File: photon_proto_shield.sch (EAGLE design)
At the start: 15 parts

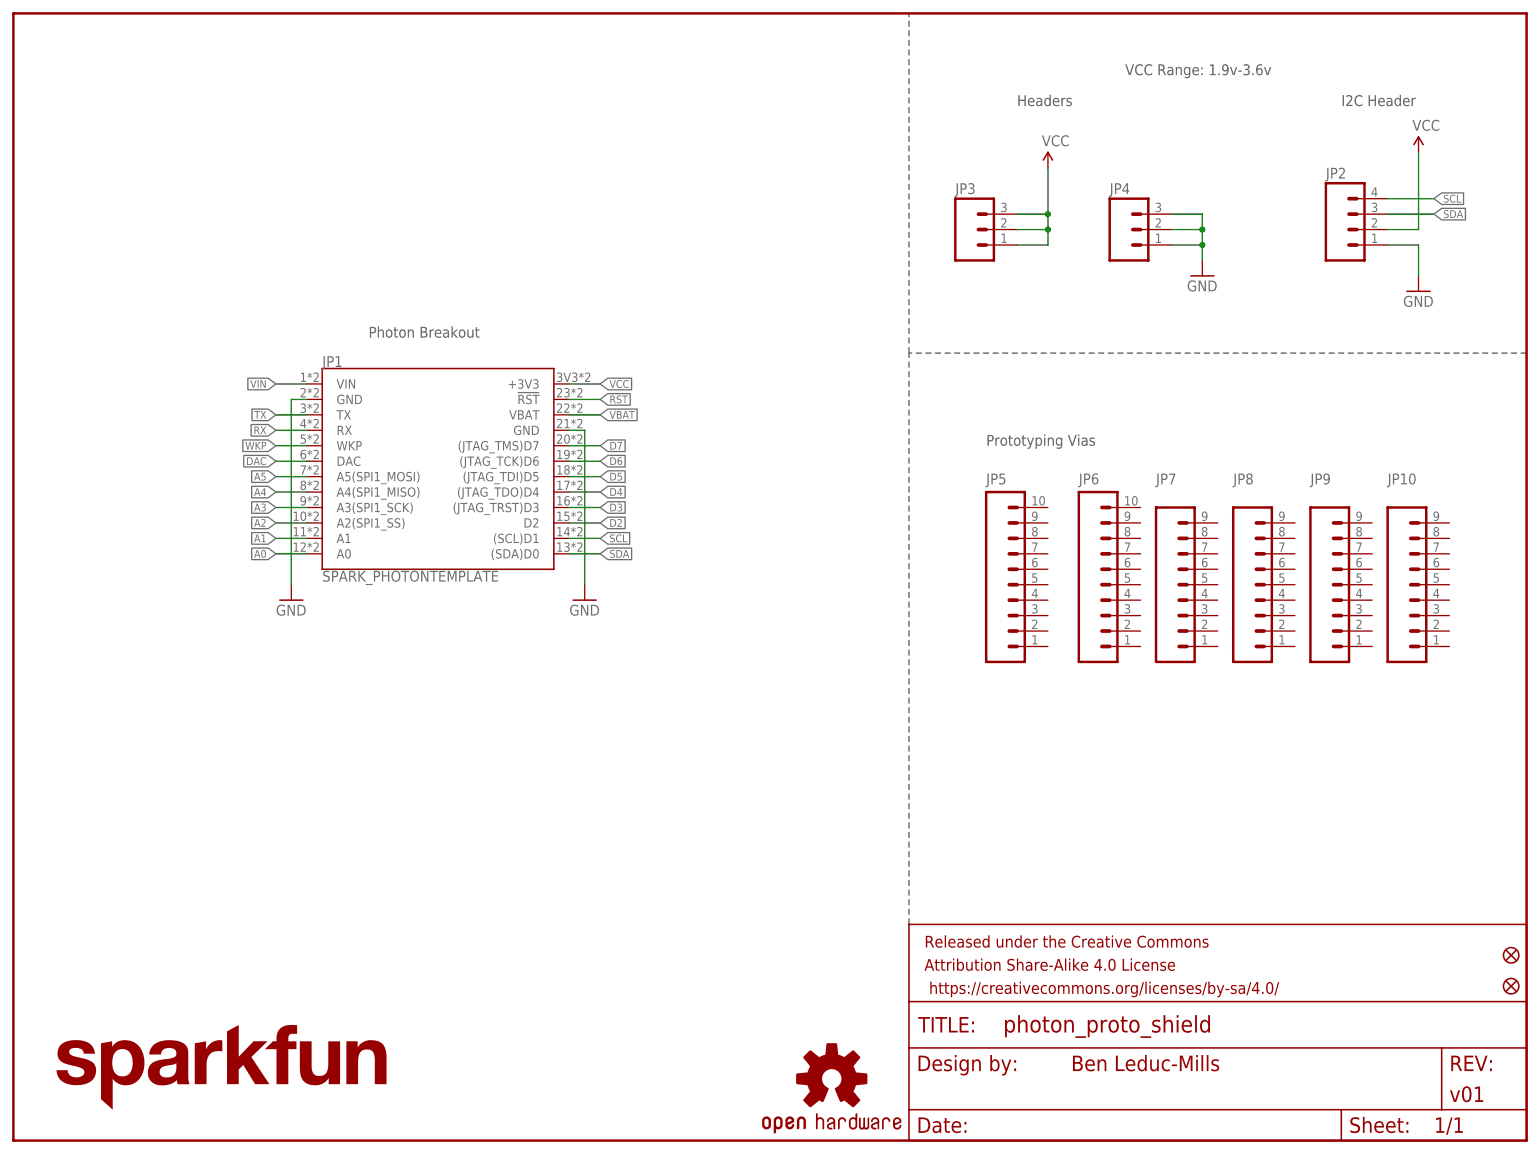
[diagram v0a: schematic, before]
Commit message: Adding gap between Photon and pin breakouts.
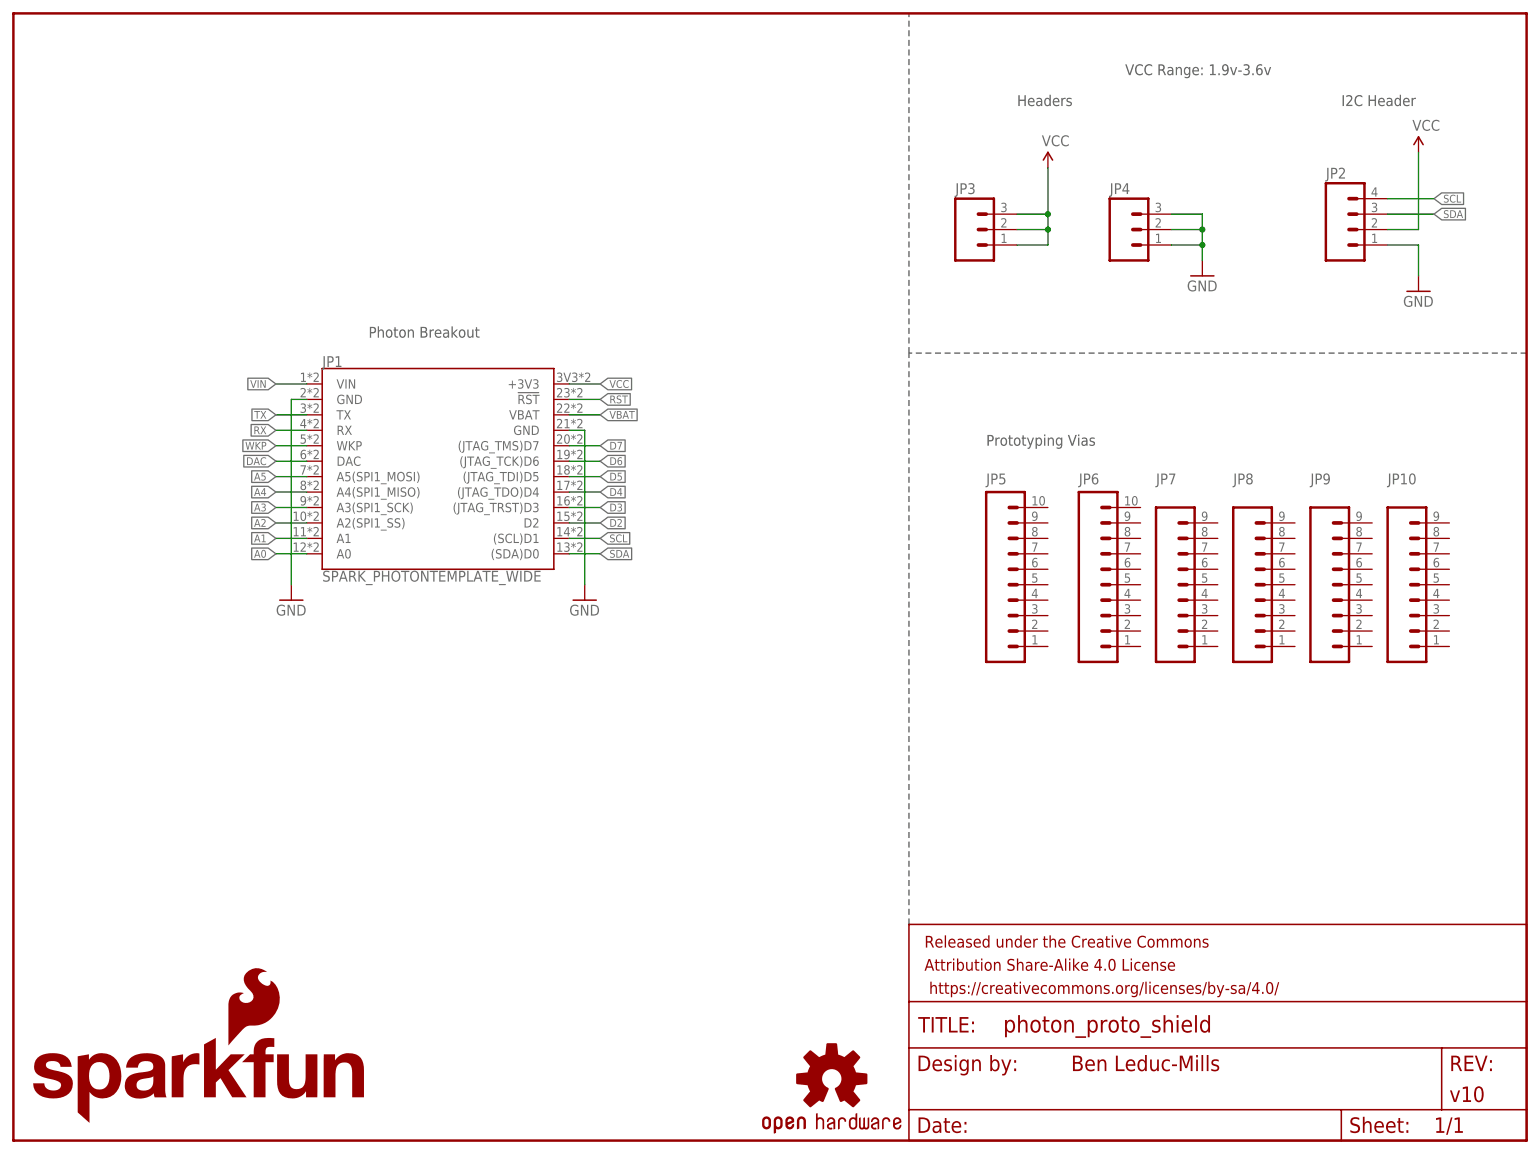
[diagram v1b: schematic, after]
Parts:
- removed FID1, FID2: FIDUCIAL1X2, SparkFun-Aesthetics:FIDUCIAL1X2
- removed LOGO3: SFE_LOGO_NAME.1_INCH, SparkFun-Aesthetics:SFE_LOGO_NAME.1_INCH
- added LOGO1: SFE_LOGO_NAME_FLAME.1_INCH, SparkFun-Aesthetics:SFE_LOGO_NAME_FLAME.1_INCH
- FRAME1: VERSION (none) -> v10
- JP1: value SPARK_PHOTONTEMPLATE -> SPARK_PHOTONTEMPLATE_WIDE; device template_temp:SPARK_PHOTONTEMPLATE -> template_temp:SPARK_PHOTONTEMPLATE_WIDE
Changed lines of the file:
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@@
 <grid distance="0.1" unitdist="inch" unit="inch" style="lines" multiple="1" display="no" altdistance="0.01" altunitdist="inch" altunit="inch"/>
 <layers>
-<layer number="1" name="Top" color="4" fill="1" visible="no" active="no"/>
-<layer number="2" name="Route2" color="1" fill="3" visible="no" active="no"/>
-<layer number="3" name="Route3" color="4" fill="3" visible="no" active="no"/>
-<layer number="4" name="Route4" color="1" fill="4" visible="no" active="no"/>
-<layer number="5" name="Route5" color="4" fill="4" visible="no" active="no"/>
-<layer number="6" name="Route6" color="1" fill="8" visible="no" active="no"/>
-<layer number="7" name="Route7" color="4" fill="8" visible="no" active="no"/>
-<layer number="8" name="Route8" color="1" fill="2" visible="no" active="no"/>
-<layer number="9" name="Route9" color="4" fill="2" visible="no" active="no"/>
-<layer number="10" name="Route10" color="1" fill="7" visible="no" active="no"/>
-<layer number="11" name="Route11" color="4" fill="7" visible="no" active="no"/>
-<layer number="12" name="Route12" color="1" fill="5" visible="no" active="no"/>
-<layer number="13" name="Route13" color="4" fill="5" visible="no" active="no"/>
-<layer number="14" name="Route14" color="1" fill="6" visible="no" active="no"/>
-<layer number="15" name="Route15" color="4" fill="6" visible="no" active="no"/>
-<layer number="16" name="Bottom" color="1" fill="1" visible="no" active="no"/>
-<layer number="17" name="Pads" color="2" fill="1" visible="no" active="no"/>
-<layer number="18" name="Vias" color="2" fill="1" visible="no" active="no"/>
-<layer number="19" name="Unrouted" color="6" fill="1" visible="no" active="no"/>
-<layer number="20" name="Dimension" color="15" fill="1" visible="no" active="no"/>
-<layer number="21" name="tPlace" color="16" fill="1" visible="no" active="no"/>
-<layer number="22" name="bPlace" color="14" fill="1" visible="no" active="no"/>
-<layer number="23" name="tOrigins" color="15" fill="1" visible="no" active="no"/>
-<layer number="24" name="bOrigins" color="15" fill="1" visible="no" active="no"/>
-<layer number="25" name="tNames" color="7" fill="1" visible="no" active="no"/>
-<layer number="26" name="bNames" color="7" fill="1" visible="no" active="no"/>
-<layer number="27" name="tValues" color="7" fill="1" visible="no" active="no"/>
-<layer number="28" name="bValues" color="7" fill="1" visible="no" active="no"/>
+<layer number="1" name="Top" color="4" fill="1" visible="yes" active="no"/>
+<layer number="2" name="Route2" color="1" fill="3" visible="yes" active="no"/>
+<layer number="3" name="Route3" color="4" fill="3" visible="yes" active="no"/>
+<layer number="4" name="Route4" color="1" fill="4" visible="yes" active="no"/>
+<layer number="5" name="Route5" color="4" fill="4" visible="yes" active="no"/>
+<layer number="6" name="Route6" color="1" fill="8" visible="yes" active="no"/>
+<layer number="7" name="Route7" color="4" fill="8" visible="yes" active="no"/>
+<layer number="8" name="Route8" color="1" fill="2" visible="yes" active="no"/>
+<layer number="9" name="Route9" color="4" fill="2" visible="yes" active="no"/>
+<layer number="10" name="Route10" color="1" fill="7" visible="yes" active="no"/>
+<layer number="11" name="Route11" color="4" fill="7" visible="yes" active="no"/>
+<layer number="12" name="Route12" color="1" fill="5" visible="yes" active="no"/>
+<layer number="13" name="Route13" color="4" fill="5" visible="yes" active="no"/>
+<layer number="14" name="Route14" color="1" fill="6" visible="yes" active="no"/>
+<layer number="15" name="Route15" color="4" fill="6" visible="yes" active="no"/>
+<layer number="16" name="Bottom" color="1" fill="1" visible="yes" active="no"/>
+<layer number="17" name="Pads" color="2" fill="1" visible="yes" active="no"/>
+<layer number="18" name="Vias" color="2" fill="1" visible="yes" active="no"/>
+<layer number="19" name="Unrouted" color="6" fill="1" visible="yes" active="no"/>
+<layer number="20" name="Dimension" color="15" fill="1" visible="yes" active="no"/>
+<layer number="21" name="tPlace" color="16" fill="1" visible="yes" active="no"/>
+<layer number="22" name="bPlace" color="14" fill="1" visible="yes" active="no"/>
+<layer number="23" name="tOrigins" color="15" fill="1" visible="yes" active="no"/>
+<layer number="24" name="bOrigins" color="15" fill="1" visible="yes" active="no"/>
+<layer number="25" name="tNames" color="7" fill="1" visible="yes" active="no"/>
+<layer number="26" name="bNames" color="7" fill="1" visible="yes" active="no"/>
+<layer number="27" name="tValues" color="7" fill="1" visible="yes" active="no"/>
+<layer number="28" name="bValues" color="7" fill="1" visible="yes" active="no"/>
 <layer number="29" name="tStop" color="7" fill="3" visible="no" active="no"/>
 <layer number="30" name="bStop" color="7" fill="6" visible="no" active="no"/>
@@
 <layer number="35" name="tGlue" color="7" fill="4" visible="no" active="no"/>
 <layer number="36" name="bGlue" color="7" fill="5" visible="no" active="no"/>
-<layer number="37" name="tTest" color="7" fill="1" visible="no" active="no"/>
-<layer number="38" name="bTest" color="7" fill="1" visible="no" active="no"/>
+<layer number="37" name="tTest" color="7" fill="1" visible="yes" active="no"/>
+<layer number="38" name="bTest" color="7" fill="1" visible="yes" active="no"/>
 <layer number="39" name="tKeepout" color="4" fill="11" visible="no" active="no"/>
 <layer number="40" name="bKeepout" color="1" fill="11" visible="no" active="no"/>
@@
 <layer number="44" name="Drills" color="7" fill="1" visible="no" active="no"/>
 <layer number="45" name="Holes" color="7" fill="1" visible="no" active="no"/>
-<layer number="46" name="Milling" color="3" fill="1" visible="no" active="no"/>
-<layer number="47" name="Measures" color="7" fill="1" visible="no" active="no"/>
-<layer number="48" name="Document" color="7" fill="1" visible="no" active="no"/>
-<layer number="49" name="Reference" color="7" fill="1" visible="no" active="no"/>
-<layer number="50" name="dxf" color="7" fill="1" visible="no" active="no"/>
-<layer number="51" name="tDocu" color="6" fill="1" visible="no" active="no"/>
-<layer number="52" name="bDocu" color="7" fill="1" visible="no" active="no"/>
-<layer number="53" name="tGND_GNDA" color="7" fill="9" visible="no" active="no"/>
-<layer number="54" name="bGND_GNDA" color="1" fill="9" visible="no" active="no"/>
-<layer number="56" name="wert" color="7" fill="1" visible="no" active="no"/>
-<layer number="57" name="tCAD" color="7" fill="1" visible="no" active="no"/>
-<layer number="59" name="tCarbon" color="7" fill="1" visible="no" active="no"/>
-<layer number="60" name="bCarbon" color="7" fill="1" visible="no" active="no"/>
+<layer number="46" name="Milling" color="3" fill="1" visible="yes" active="no"/>
+<layer number="47" name="Measures" color="7" fill="1" visible="yes" active="no"/>
+<layer number="48" name="Document" color="7" fill="1" visible="yes" active="no"/>
+<layer number="49" name="Reference" color="7" fill="1" visible="yes" active="no"/>
+<layer number="50" name="dxf" color="7" fill="1" visible="yes" active="no"/>
+<layer number="51" name="tDocu" color="6" fill="1" visible="yes" active="no"/>
+<layer number="52" name="bDocu" color="7" fill="1" visible="yes" active="no"/>
+<layer number="53" name="tGND_GNDA" color="7" fill="9" visible="yes" active="no"/>
+<layer number="54" name="bGND_GNDA" color="1" fill="9" visible="yes" active="no"/>
+<layer number="56" name="wert" color="7" fill="1" visible="yes" active="no"/>
+<layer number="57" name="tCAD" color="7" fill="1" visible="yes" active="no"/>
+<layer number="59" name="tCarbon" color="7" fill="1" visible="yes" active="no"/>
+<layer number="60" name="bCarbon" color="7" fill="1" visible="yes" active="no"/>
 <layer number="90" name="Modules" color="5" fill="1" visible="yes" active="yes"/>
 <layer number="91" name="Nets" color="2" fill="1" visible="yes" active="yes"/>
@@
 <part name="FRAME1" library="SparkFun-Aesthetics" deviceset="FRAME-LETTER" device="">
 <attribute name="DESIGNER" value="Ben Leduc-Mills"/>
+<attribute name="VERSION" value="v10"/>
 </part>
-<part name="JP1" library="template_temp" deviceset="SPARK_PHOTON" device="TEMPLATE" value="SPARK_PHOTONTEMPLATE"/>
+<part name="JP1" library="template_temp" deviceset="SPARK_PHOTON" device="TEMPLATE_WIDE" value="SPARK_PHOTONTEMPLATE_WIDE"/>
 <part name="GND1" library="SparkFun-Aesthetics" deviceset="GND" device=""/>
 <part name="GND2" library="SparkFun-Aesthetics" deviceset="GND" device=""/>
 <part name="LOGO2" library="SparkFun-Aesthetics" deviceset="OSHW-LOGO" device="S"/>
-<part name="LOGO3" library="SparkFun-Aesthetics" deviceset="SFE_LOGO_NAME" device=".1_INCH"/>
-<part name="FID1" library="SparkFun-Aesthetics" deviceset="FIDUCIAL" device="1X2"/>
-<part name="FID2" library="SparkFun-Aesthetics" deviceset="FIDUCIAL" device="1X2"/>
 <part name="JP2" library="SparkFun-Connectors" deviceset="M04" device="PTH"/>
 <part name="JP3" library="SparkFun-Connectors" deviceset="M03" device="PTH"/>
@@
 <part name="JP9" library="SparkFun-Connectors" deviceset="M09" device="NO_SILK"/>
 <part name="JP10" library="SparkFun-Connectors" deviceset="M09" device="NO_SILK"/>
+<part name="LOGO1" library="SparkFun-Aesthetics" deviceset="SFE_LOGO_NAME_FLAME" device=".1_INCH"/>
 </parts>
 <sheets>
@@
 <instance part="GND2" gate="1" x="93.98" y="88.9"/>
 <instance part="LOGO2" gate="G$1" x="134.62" y="10.16"/>
-<instance part="LOGO3" gate="G$1" x="5.08" y="5.08"/>
-<instance part="FID1" gate="G$1" x="246.38" y="30.48"/>
-<instance part="FID2" gate="G$1" x="246.38" y="25.4"/>
 <instance part="JP2" gate="G$1" x="220.98" y="149.86"/>
 <instance part="JP3" gate="G$1" x="157.48" y="149.86"/>
@@
 <instance part="JP9" gate="G$1" x="213.36" y="91.44"/>
 <instance part="JP10" gate="G$1" x="226.06" y="91.44"/>
+<instance part="LOGO1" gate="G$1" x="2.54" y="2.54"/>
 </instances>
 <busses>
